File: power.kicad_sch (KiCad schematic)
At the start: 20 parts, among them U2 AOZ1280CI, U3 LM1117-5.0, U4 LM1117-3.3, U5 LM321

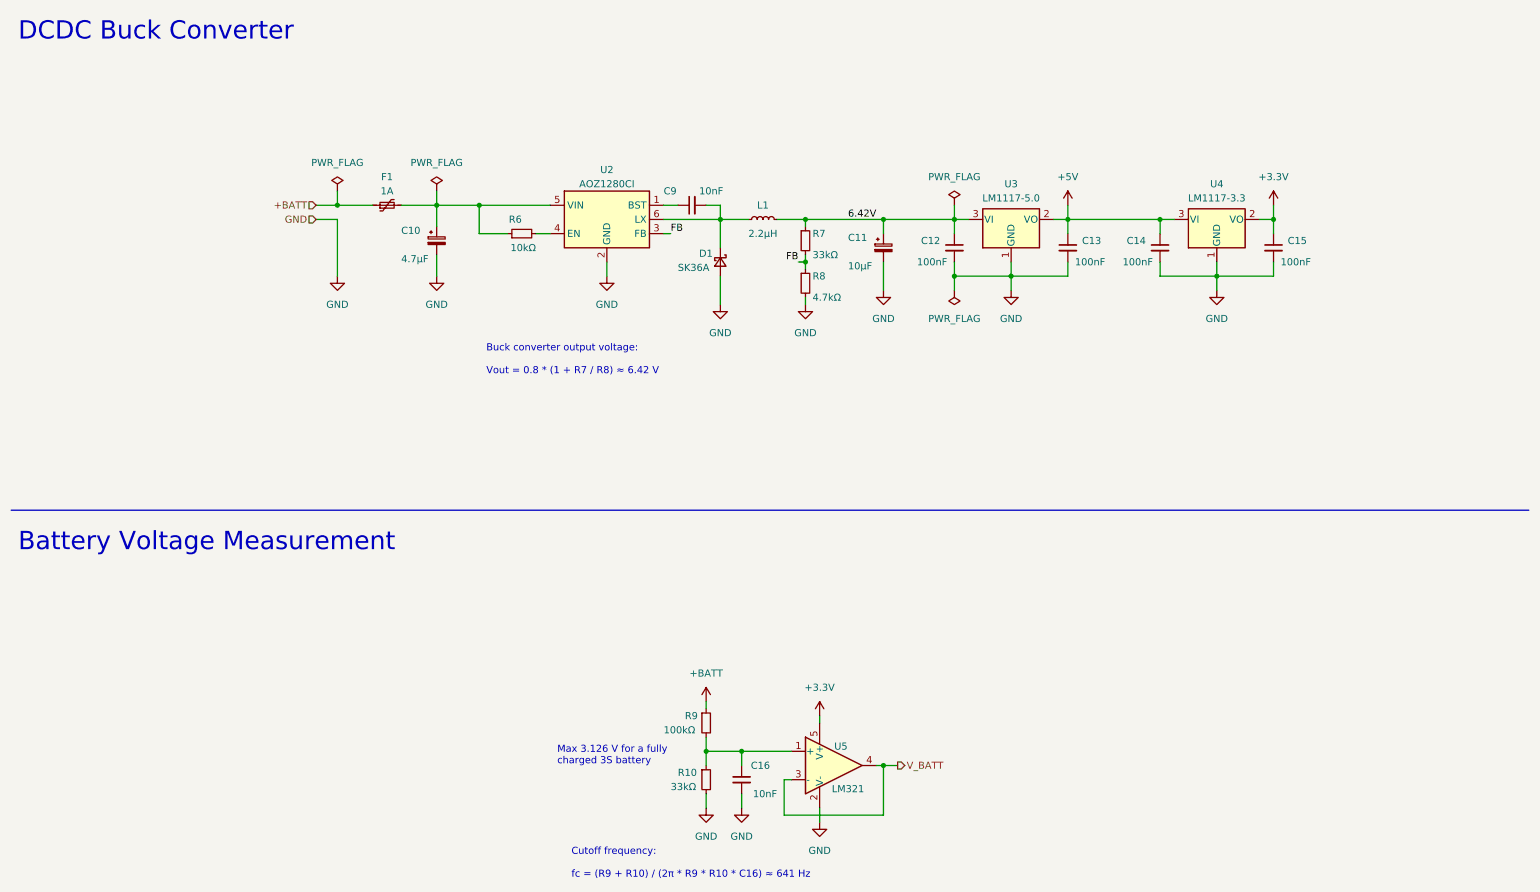
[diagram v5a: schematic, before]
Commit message: Remove 5V LDO regulator
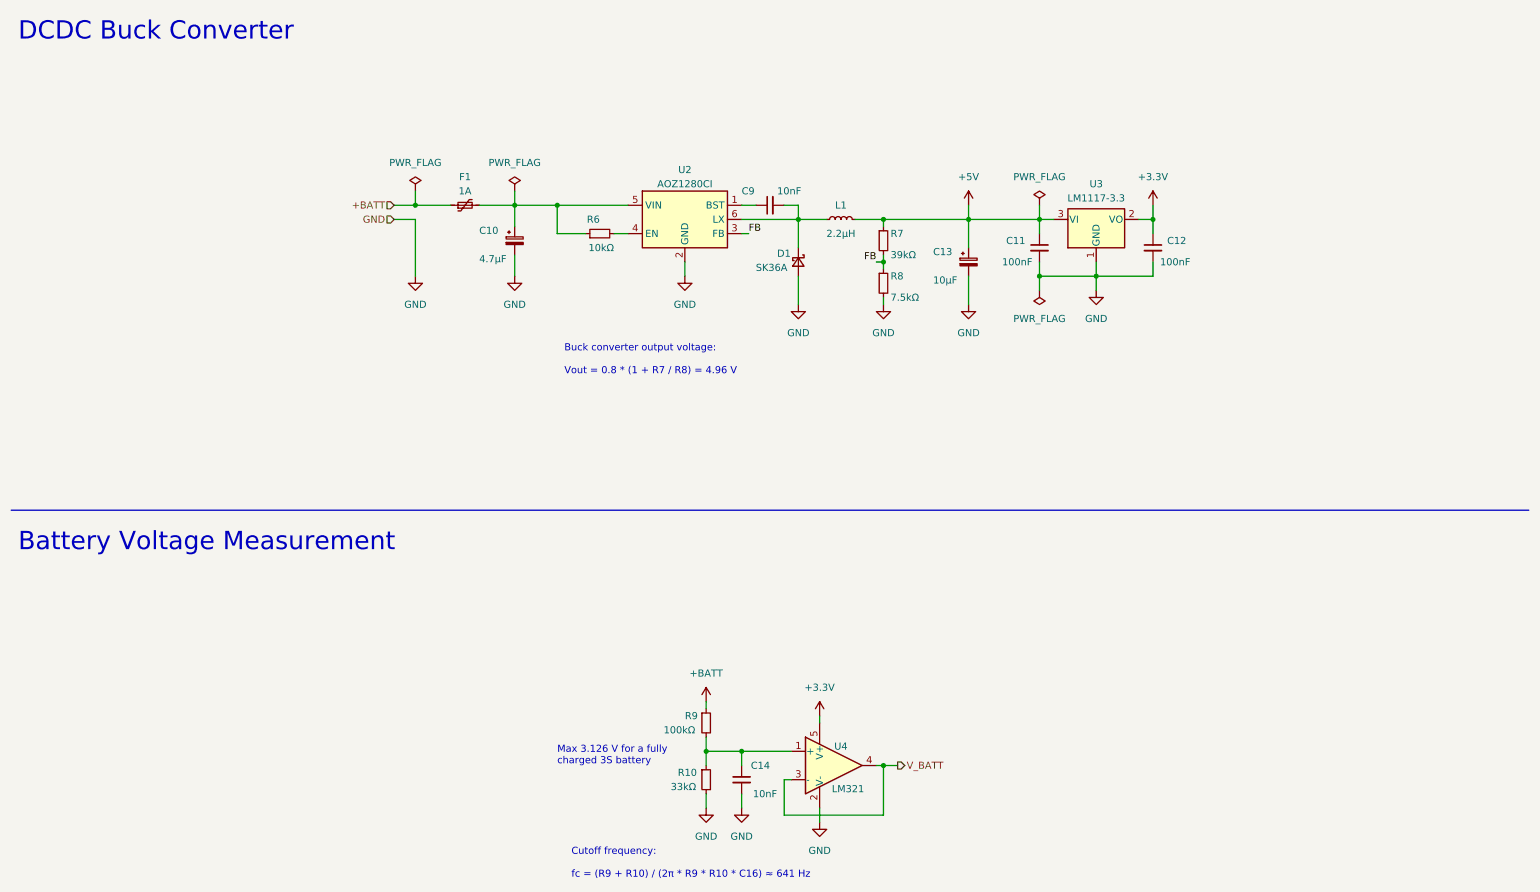
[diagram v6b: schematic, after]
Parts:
- removed C14, C15: 100nF, Capacitor_SMD:C_0603_1608Metric, symbol Device:C_Small
- removed U3: LM1117-5.0, Package_TO_SOT_SMD:SOT-223-3_TabPin2, symbol Regulator_Linear:LM1117-5.0
- R7: value 33kΩ -> 39kΩ
- R8: value 4.7kΩ -> 7.5kΩ
- renumbered C12 to C11, C13 to C12, C11 to C13, C16 to C14, U4 to U3, U5 to U4
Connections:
- net 6.42V is gone; now on net +5V: C11.1, C13.1, L1.2, R7.1
- net +3.3V: now also C12.1
- net +5V: no longer C12.1
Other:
- note added: "Buck converter output voltage: Vout = 0.8 * (1 + R7 / R8) = 4.96 V"
- note removed: "Buck converter output voltage: Vout = 0.8 * (1 + R7 / R8) ≈ 6.42 V"
- moved on the sheet: C10, C11, C12, C13, C9, D1, F1, L1, R6, R7, R8, U2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

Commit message: Arrange footprints
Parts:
- added C12: 10μF, Capacitor_Tantalum_SMD:CP_EIA-3216-10_Kemet-I, symbol Device:C_Polarized_Small
- renumbered C13 to C11, C11 to C13, C12 to C14, C14 to C15
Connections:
- net +5V: now also C12.1
- net GND: now also C12.2
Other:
- note added: "Cutoff frequency: fc = (R9 + R10) / (2π * R9 * R10 * C15) ≈ 641 Hz"
- note removed: "Cutoff frequency: fc = (R9 + R10) / (2π * R9 * R10 * C16) ≈ 641 Hz"
- company: (none) -> Authors: H. Fedarovich, I. Kajdan
- moved on the sheet: C10, C11, C13, C14, C9, D1, F1, L1, R6, R7, R8, U2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
